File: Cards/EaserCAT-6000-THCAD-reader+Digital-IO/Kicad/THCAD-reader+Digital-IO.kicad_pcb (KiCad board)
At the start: 2 copper layers, 112.5 x 65.6 mm, 138 parts, among them CN1 10pF, CN2 10pF, CN3 0.1uF, J1 In1-4, J10 Output3-4, J11 5V input, J2 In5-8, J3 In9-12, J4 24V_Common, J5 Serial usart1, J6 THCAD, J7 STLINK, J8 Output1-2, J9 24V Field, SW1 SW_Push, U1 TLP292-4, U2 AT24CS32-SSHM, U3 TLP292-4, U4 TLP292-4, U5 LAN9252_PT, U6 STM32F407VGT6, U7 MAX3485CSA/ESA, U8 TLP292-4, U9 AMS1117-3.3, Y1 25MHz, Y2 8 MHz

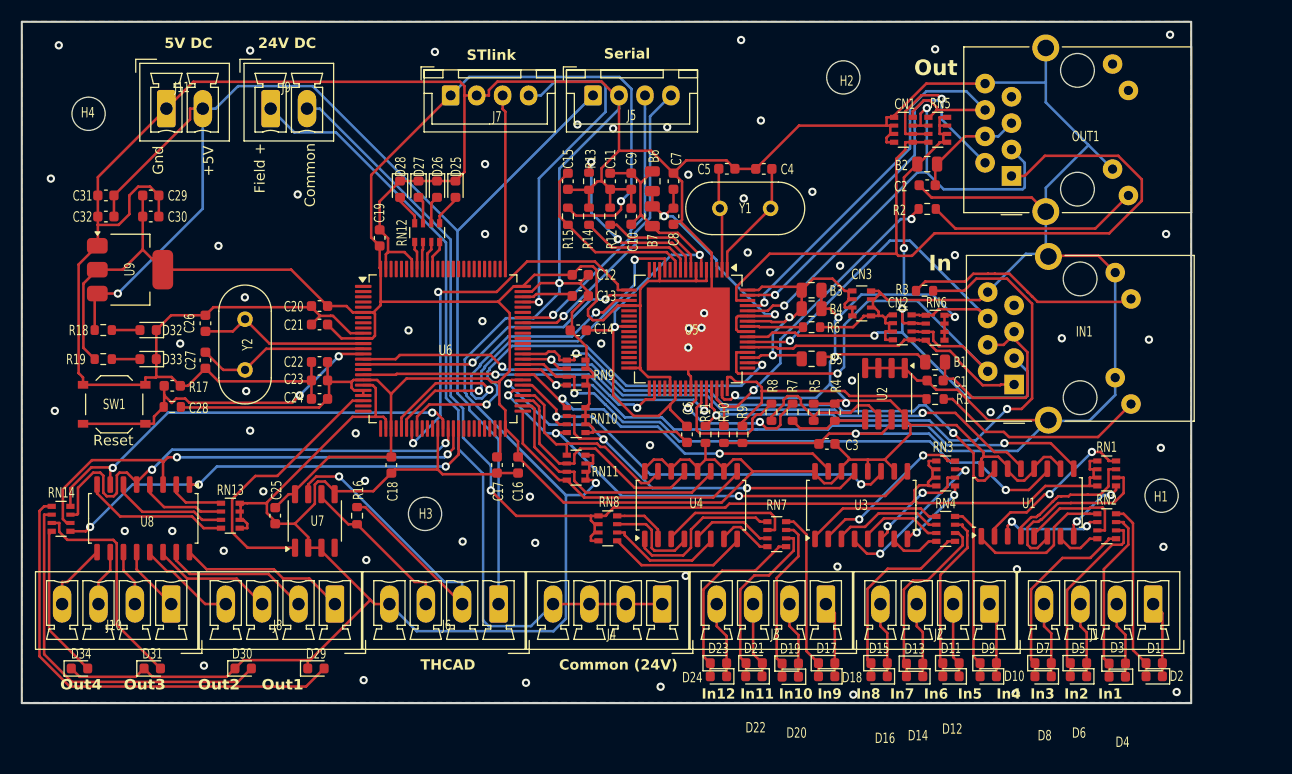
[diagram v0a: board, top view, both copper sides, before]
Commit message: Modified, switch marker postions for C28 and R17
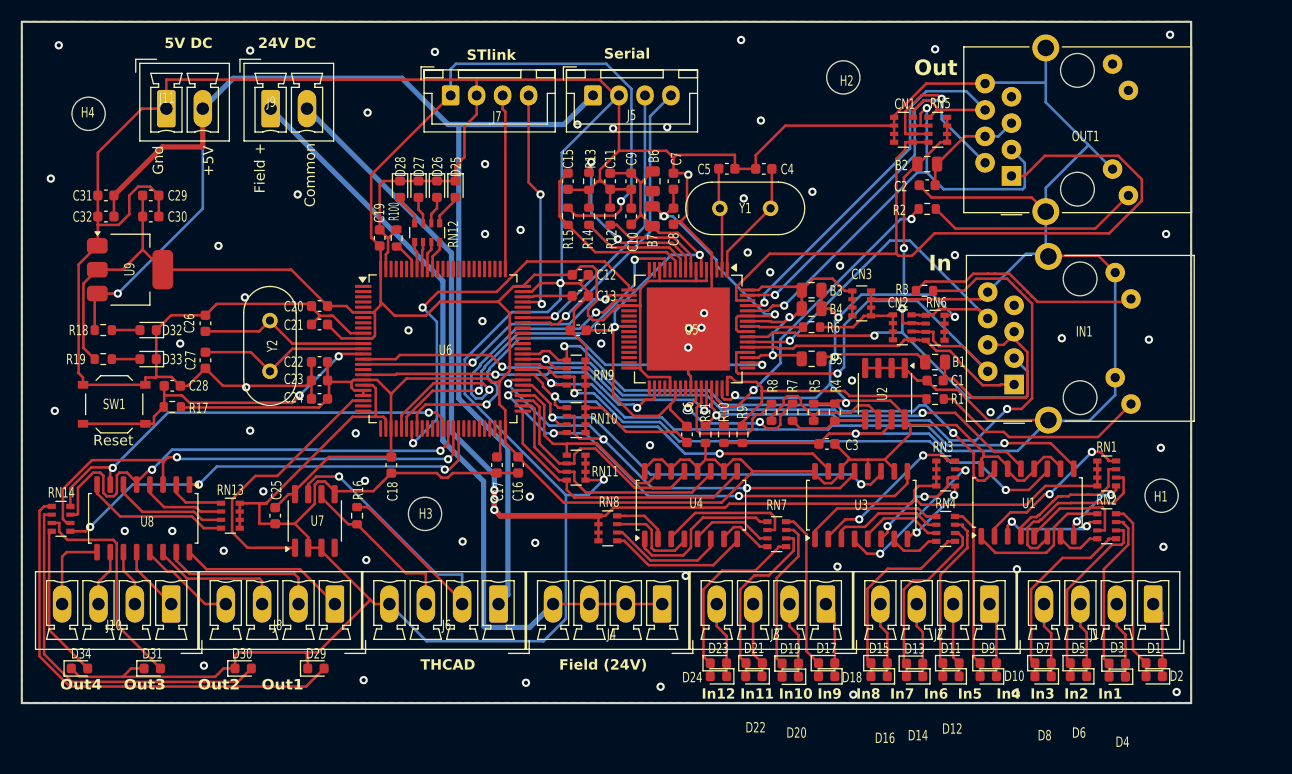
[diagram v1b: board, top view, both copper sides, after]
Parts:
- added R100: 100k, Resistor_SMD:R_0603_1608Metric, F.Cu at (175.8, 116.1)
- R18: value 2k -> 4k7
- moved Y2 2.40 mm to (163.6, 128.9)
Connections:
- U6 pad 37: GND -> unconnected-(U6-PB2-Pad37)
- U6 pad 94: GND -> Net-(U6-BOOT0)
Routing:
- net SWDIO: track 33.1 -> 22.5 mm, vias 1 -> 2
- net +5V: track 128.6 -> 133.2 mm
- net 24V_COMMON: track 121.8 -> 118.6 mm, vias 1 -> 3
- net Net-(U6-BOOT0): track 0.00 -> 2.86 mm
- net 24V_FIELD: track 78.4 -> 76.4 mm
- net Net-(J8-Pin_2): track 14.3 -> 15.8 mm
- net GND: track 657.3 -> 658.8 mm, vias 66 -> 67
- net Net-(J10-Pin_4): track 6.68 -> 8.10 mm
- net +3.3V: track 413.3 -> 414.7 mm
- net +3.3VA: track 32.4 -> 31.0 mm
- net Net-(J8-Pin_3): track 11.7 -> 13.0 mm
- net IN0: track 54.0 -> 55.3 mm
- net IN4: track 34.5 -> 35.5 mm
- net SPI_MOSI: track 38.2 -> 39.1 mm
- net SPI_CS: track 43.8 -> 42.9 mm
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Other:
- board text added: "EaserCAT 6000 MetalMusings January 2025"
- board text added: "Field (24V)"
- board text removed: "Common (24V)"
- board text removed: "EaserCAT 6000 MetalMusings December 2024"

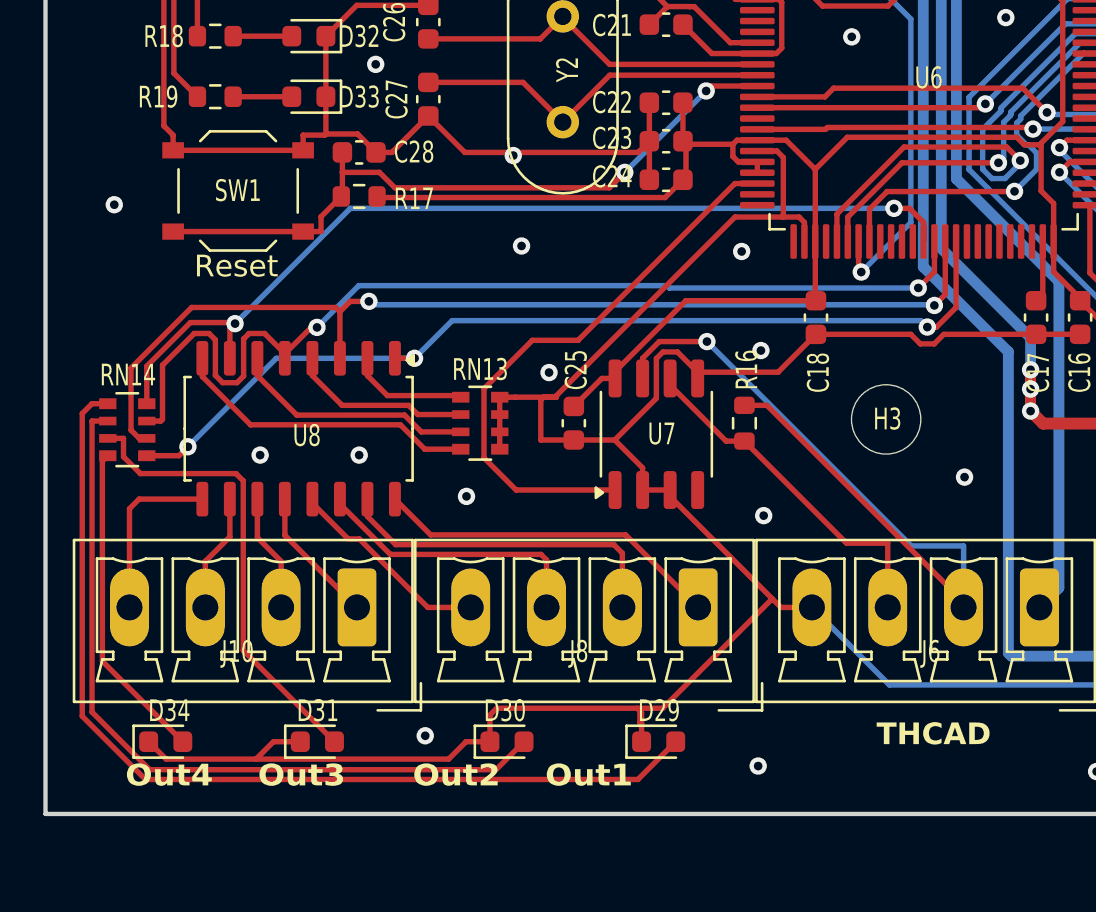
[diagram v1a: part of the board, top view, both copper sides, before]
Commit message: Fixed placement of Out1-Out4 diodes' marking
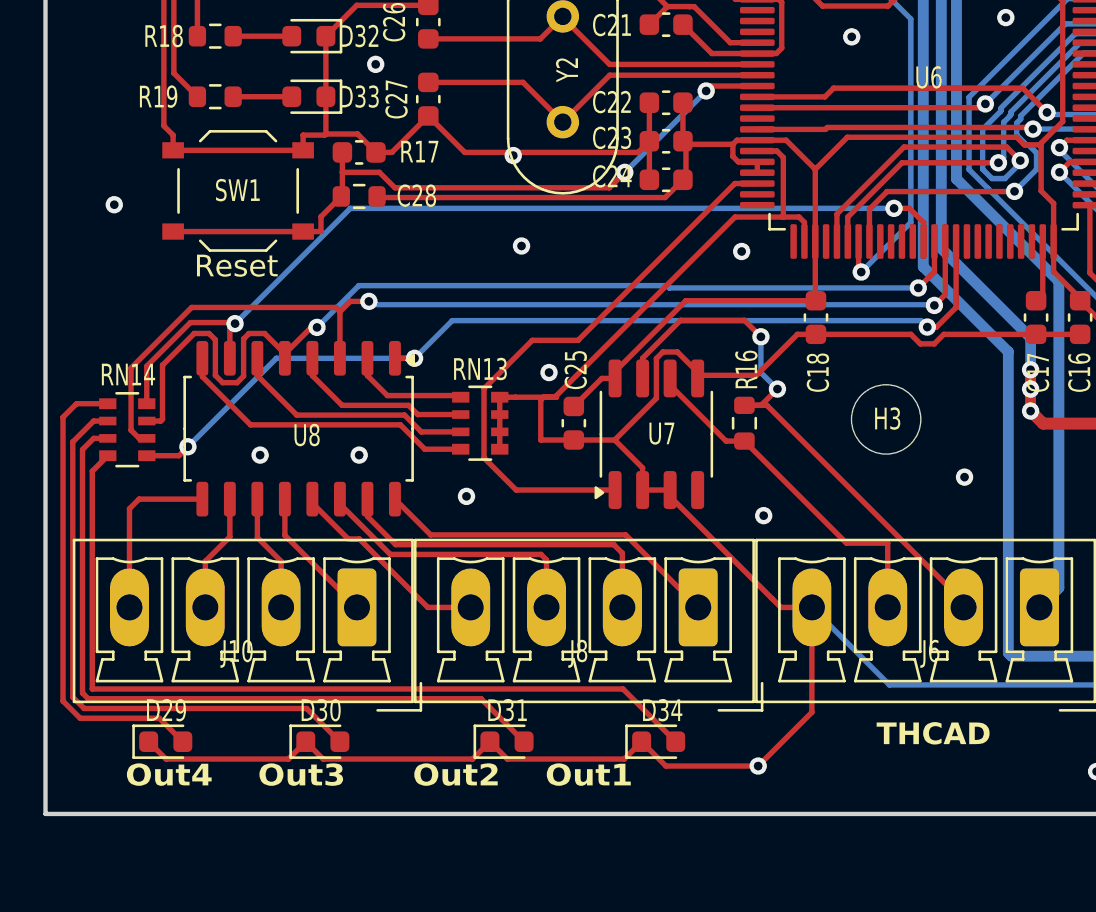
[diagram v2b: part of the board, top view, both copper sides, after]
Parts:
- moved D29 22.8 mm to (145.2, 157.5)
- moved D34 22.8 mm to (168.0, 157.5)
- moved D31 8.75 mm to (161.0, 157.5)
- moved D30 8.50 mm to (152.5, 157.5)
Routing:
- net Net-(D34-A): track 14.8 -> 39.0 mm
- net Net-(D29-A): track 44.7 -> 21.7 mm
- net Net-(D31-A): track 21.3 -> 33.9 mm
- net A: track 36.9 -> 26.1 mm, vias 1 -> 2
- net Net-(D30-A): track 35.7 -> 27.0 mm
- net GND: track 658.8 -> 660.3 mm, vias 67 -> 65
